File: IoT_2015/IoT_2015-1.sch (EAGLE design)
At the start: 28 parts, among them Y1 ABLS-16.000MHZ-B4-T

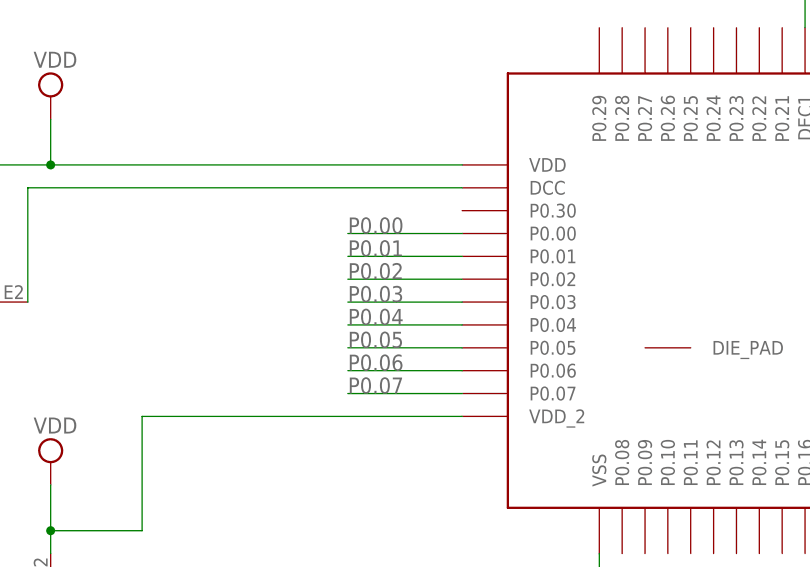
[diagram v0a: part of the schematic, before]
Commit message: Routed by hand
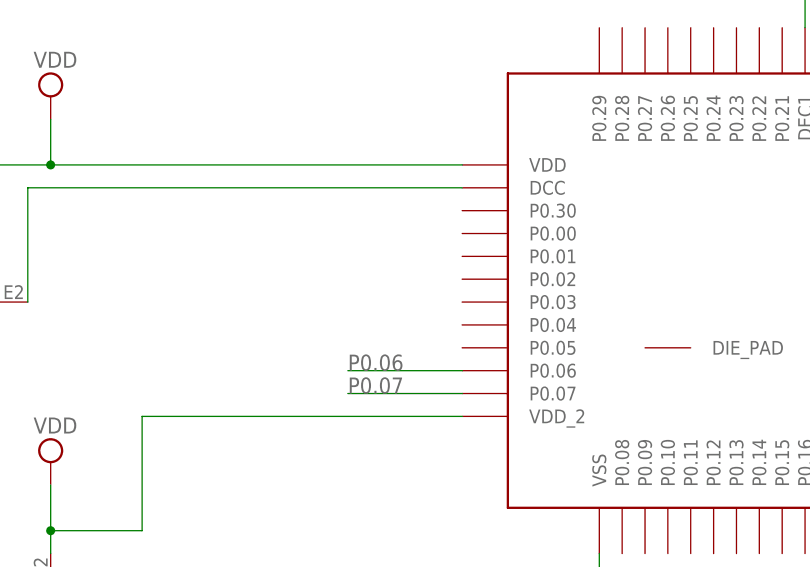
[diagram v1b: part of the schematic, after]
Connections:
- removed net P0.00: U$1.P0.00
- removed net P0.01: U$1.P0.01
- removed net P0.02: U$1.P0.02
- removed net P0.03: U$1.P0.03
- removed net P0.04: U$1.P0.04
- removed net P0.05: U$1.P0.05
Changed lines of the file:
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@@
-</segment>
-</net>
-<net name="P0.00" class="0">
-<segment>
-<pinref part="U$1" gate="G$1" pin="P0.00"/>
-<wire x1="68.58" y1="53.34" x2="55.88" y2="53.34" width="0.1524" layer="91"/>
-<label x="55.88" y="53.34" size="1.778" layer="95"/>
-</segment>
-</net>
-<net name="P0.01" class="0">
-<segment>
-<pinref part="U$1" gate="G$1" pin="P0.01"/>
-<wire x1="68.58" y1="50.8" x2="55.88" y2="50.8" width="0.1524" layer="91"/>
-<label x="55.88" y="50.8" size="1.778" layer="95"/>
-</segment>
-</net>
-<net name="P0.02" class="0">
-<segment>
-<pinref part="U$1" gate="G$1" pin="P0.02"/>
-<wire x1="68.58" y1="48.26" x2="55.88" y2="48.26" width="0.1524" layer="91"/>
-<label x="55.88" y="48.26" size="1.778" layer="95"/>
-</segment>
-</net>
-<net name="P0.03" class="0">
-<segment>
-<pinref part="U$1" gate="G$1" pin="P0.03"/>
-<wire x1="68.58" y1="45.72" x2="55.88" y2="45.72" width="0.1524" layer="91"/>
-<label x="55.88" y="45.72" size="1.778" layer="95"/>
-</segment>
-</net>
-<net name="P0.04" class="0">
-<segment>
-<pinref part="U$1" gate="G$1" pin="P0.04"/>
-<wire x1="68.58" y1="43.18" x2="55.88" y2="43.18" width="0.1524" layer="91"/>
-<label x="55.88" y="43.18" size="1.778" layer="95"/>
-</segment>
-</net>
-<net name="P0.05" class="0">
-<segment>
-<pinref part="U$1" gate="G$1" pin="P0.05"/>
-<wire x1="68.58" y1="40.64" x2="55.88" y2="40.64" width="0.1524" layer="91"/>
-<label x="55.88" y="40.64" size="1.778" layer="95"/>
 </segment>
 </net>
